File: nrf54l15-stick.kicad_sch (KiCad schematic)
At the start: 29 parts, among them J1 USB_A, J2 programming conn, J3 Conn_01x04_Pin, SW4 SW_Push, SW5 SW_Push, SW6 Processor_reset, U3 APX803L20-29C3-7, U4 CP2102C-Axx-xQFN24, U5 BM15C, Y1 32.768kHz

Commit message: shrunk, routed, passes drc, no checklist yet
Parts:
- removed C4: 4.7uF/10V, Capacitor_SMD:C_0805_2012Metric, symbol Device:C
- removed J3: Conn_01x04_Pin, footprint:UART-sot, symbol Connector:Conn_01x04_Pin
- removed SW5: SW_Push, footprint:SW_STU-057A23AC_8127_2.25N, symbol custom comp:SW_Push
- removed SW6: Processor_reset, footprint:SW_STU-057A23AC_8127_2.25N, symbol custom comp:SW_Push
- added C8: 4.7uF/10V, Capacitor_SMD:C_0603_1608Metric, symbol Device:C
- added FID4, FID5, FID6: Fiducial, Fiducial:Fiducial_0.5mm_Mask1mm, symbol Mechanical:Fiducial
- C16: value 0.10uF/50V/0402 -> 0.10uF/50v; MFR Samsung -> (none); MFR_PN CL10B104KB8NNWC -> (none)
- C20: value 0.10uF/50V/0603 -> 0.10uF/50v; footprint Capacitor_SMD:C_0603_1608Metric -> Capacitor_SMD:C_0402_1005Metric; MFR Samsung -> (none); MFR_PN CL10B104KB8NNWC -> (none)
- C7: footprint Capacitor_SMD:C_0805_2012Metric -> Capacitor_SMD:C_0603_1608Metric; MFR Samsung -> (none); MFR_PN CL21A475KPFNNNE -> (none)
- D7, D8: footprint LED_SMD:LED_0805_2012Metric -> footprint:LED_0805_2012Metric
- FID1, FID2, FID3: footprint Fiducial:Fiducial_1mm_Mask2mm -> Fiducial:Fiducial_0.5mm_Mask1mm
- R15: footprint Capacitor_SMD:C_0603_1608Metric -> Resistor_SMD:R_0603_1608Metric; MFR Stackpole Electronics Inc -> (none); MFR_PN RMCF0805FT47R0 -> (none)
- R16: MFR Stackpole Electronics Inc -> (none); MFR_PN RMCF0805FT270R -> (none)
- R17: value 100K/0603 -> 100K; footprint Resistor_SMD:R_0603_1608Metric -> Resistor_SMD:R_0402_1005Metric; MFR Stackpole Electronics Inc -> (none); MFR_PN RMCF0603FT100K -> (none)
- R29: value 1.00K/0603 -> 1.00K; footprint Resistor_SMD:R_0603_1608Metric -> Resistor_SMD:R_0402_1005Metric; MFR Stackpole Electronics Inc -> (none); MFR_PN RMCF0603FT100K -> (none)
- R7: value 1k/0603 -> 1.00k; footprint Resistor_SMD:R_0603_1608Metric -> Resistor_SMD:R_0402_1005Metric; MFR Stackpole Electronics Inc -> (none); MFR_PN RMCF0603FT1K00 -> (none)
- R8: value 22.1k/0603 -> 22.1k; footprint Resistor_SMD:R_0603_1608Metric -> Resistor_SMD:R_0402_1005Metric; MFR Stackpole Electronics Inc -> (none); MFR_PN RMCF0603FT22K1 -> (none)
- R9: value 47.5k/0603 -> 47.5k; footprint Resistor_SMD:R_0603_1608Metric -> Resistor_SMD:R_0402_1005Metric; MFR Stackpole Electronics Inc -> (none); MFR_PN RMCF0603FT47K5 -> (none)
- SW4: MFR TE Connectivity -> (none); MFR_PN FSM6JSMATR -> (none)
- U3: value APX803L20-29C3-7 -> APX803L20-27SR-7; MFR_PN APX803L20-29C3-7 -> APX803L20-27SR-7
- U4: footprint Package_DFN_QFN:WQFN-24-1EP_4x4mm_P0.5mm_EP2.45x2.45mm -> footprint:QFN-24-1EP_4x4mm_P0.5mm_EP2.5x2.5mm
- U5: MFR Fanstel -> (none); MFR_PN BM15C -> (none)
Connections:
- net +5V: now also C8.2
- net GND: now also C8.1
- net BUTTON1: no longer names the net of U5.J2 (P0.03)
- net I2C_SCL: no longer names the net of U5.E9 (P1.04/AIN0)
- net I2C_SDA: no longer names the net of U5.E8 (P1.03)
- net P1.09: no longer names the net of U5.A3 (P1.09)
- net P1.11/AIN4: no longer names the net of U5.B3 (P1.11/AIN4)
- net P1.12/AIN5: no longer names the net of U5.B4 (P1.12/AIN5)
- net P1.13/AIN6: no longer names the net of U5.B5 (P1.13/AIN6)
- net P1.14/AIN7: no longer names the net of U5.B6 (P1.14/AIN7)
- net PWM_CH_X: no longer names the net of U5.G9 (P1.07/AIN3)
- net PWM_CH_Y: no longer names the net of U5.G8 (P1.08)
- net UART_RX renamed UART_nRF_RX
- net UART_nRF_RX: now also U4.21 (TXD); no longer U4.20 (RXD)
- net UART_TX renamed UART_nRF_TX
- net UART_nRF_TX: now also U4.20 (RXD); no longer U4.21 (TXD)
- no-connect marks 0 -> 35
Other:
- moved on the sheet: C16, C20, C7, FID3, J1, R17, R29, R7, R8, R9, SW4, U4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

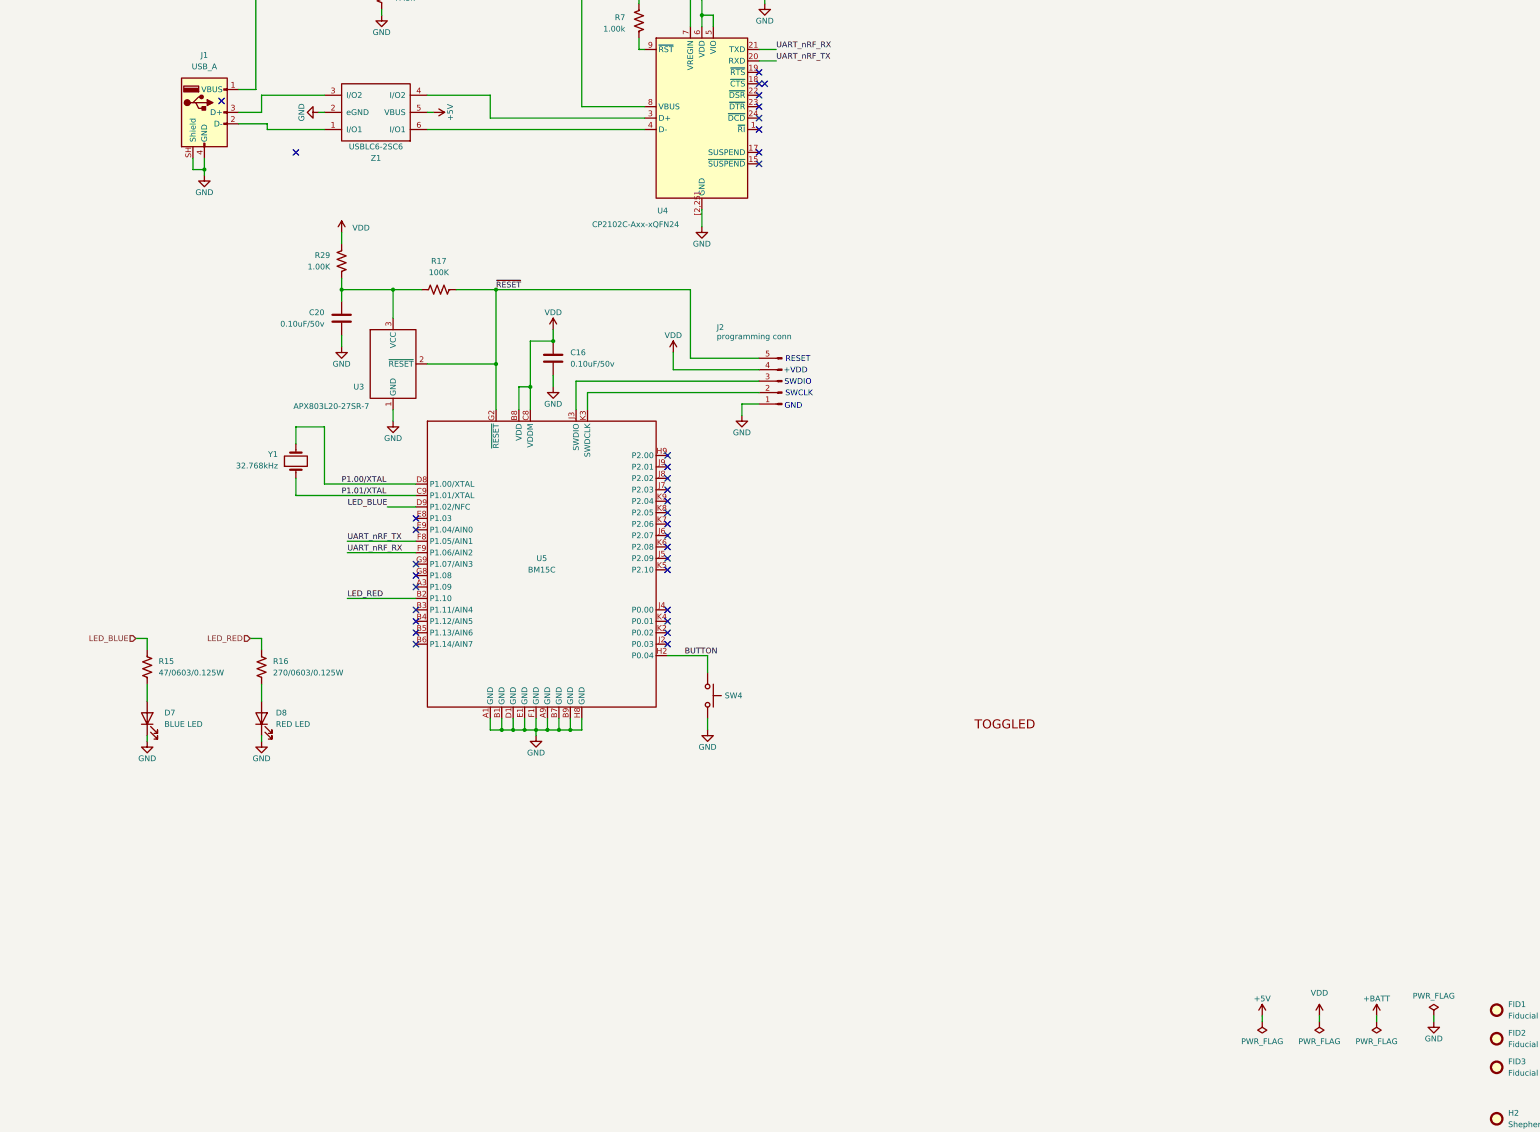
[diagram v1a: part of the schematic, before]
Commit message: fixed design net rules, passes drc
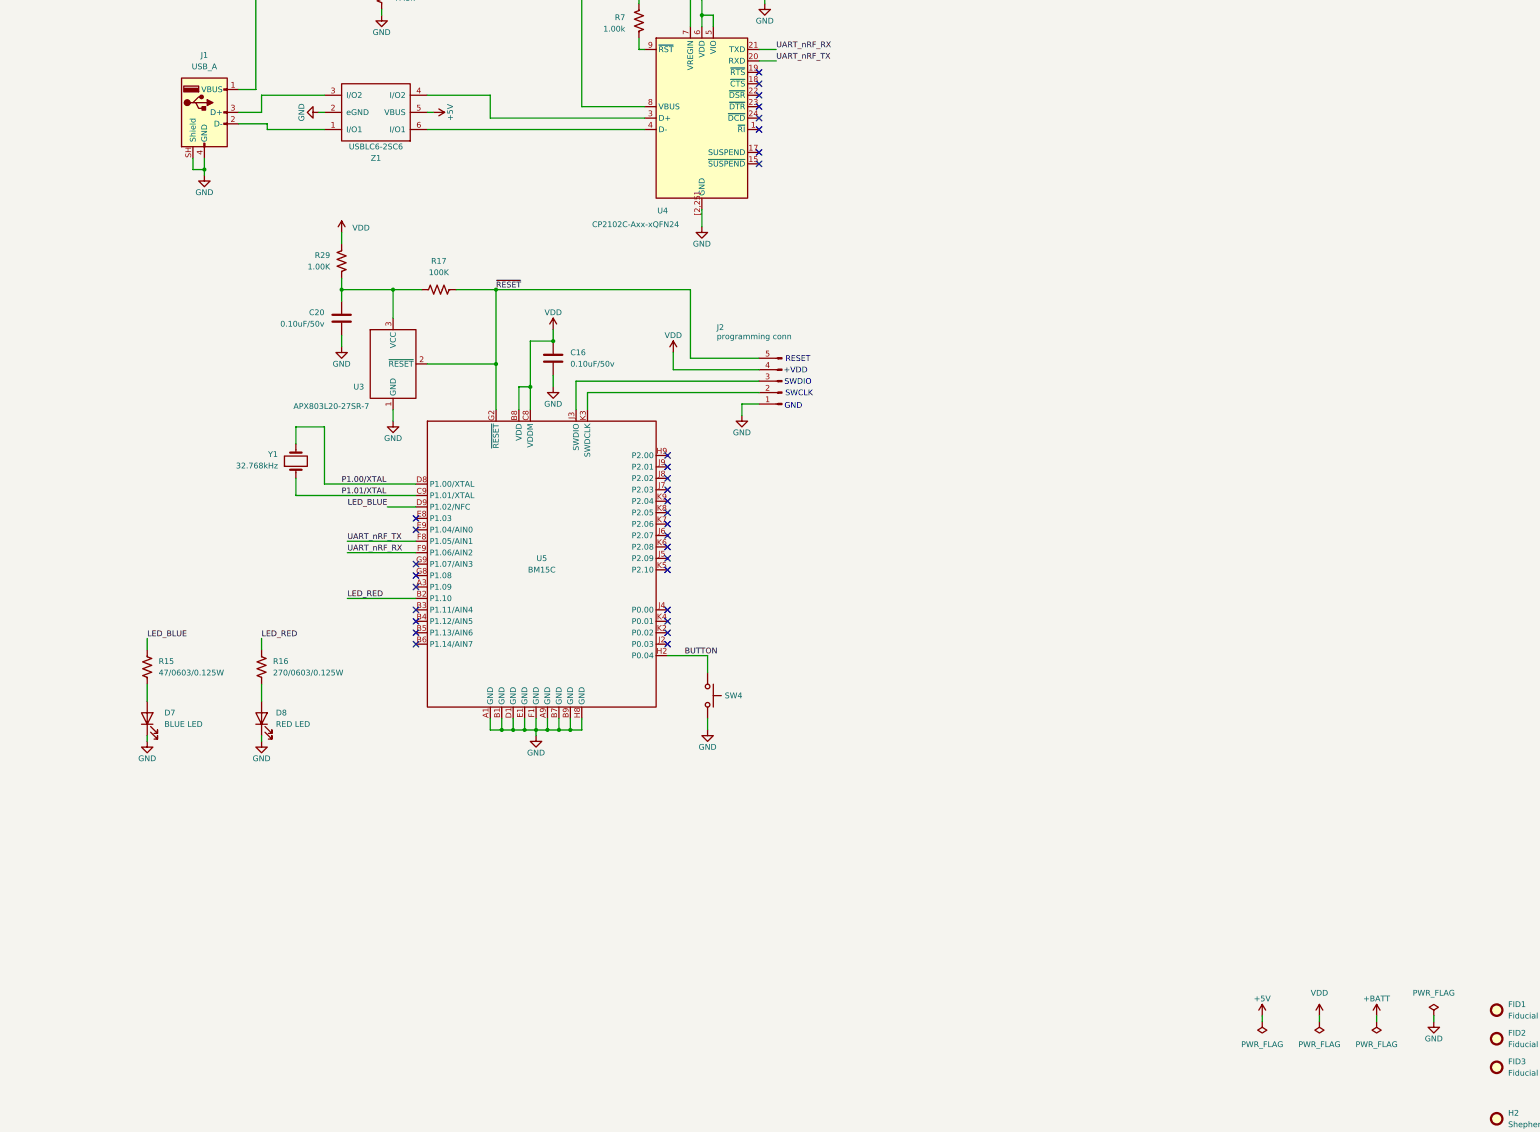
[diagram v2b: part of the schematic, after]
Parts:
- removed L1: toggled, footprint:toggled, symbol custom comp:toggled
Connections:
- no-connect marks 35 -> 32
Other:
- title: Fanstel BM15C Breakout Board | 62-02298 -> (none)
